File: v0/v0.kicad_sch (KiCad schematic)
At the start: 43 parts, among them CON1 SNES-CONN, M1 LY68L6400SLIT, U1 SN74LV165APWR, U2 SN74LV165APWR, U3 SN74LV165APWR, U4 SN74LVC8T245PWR, U5 PIC12F629-I/SN, U6 AMS1117-3.3, U7 SN74LVC8T245PWR, U8 Pair of 20-pin 1.27mm pitch v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

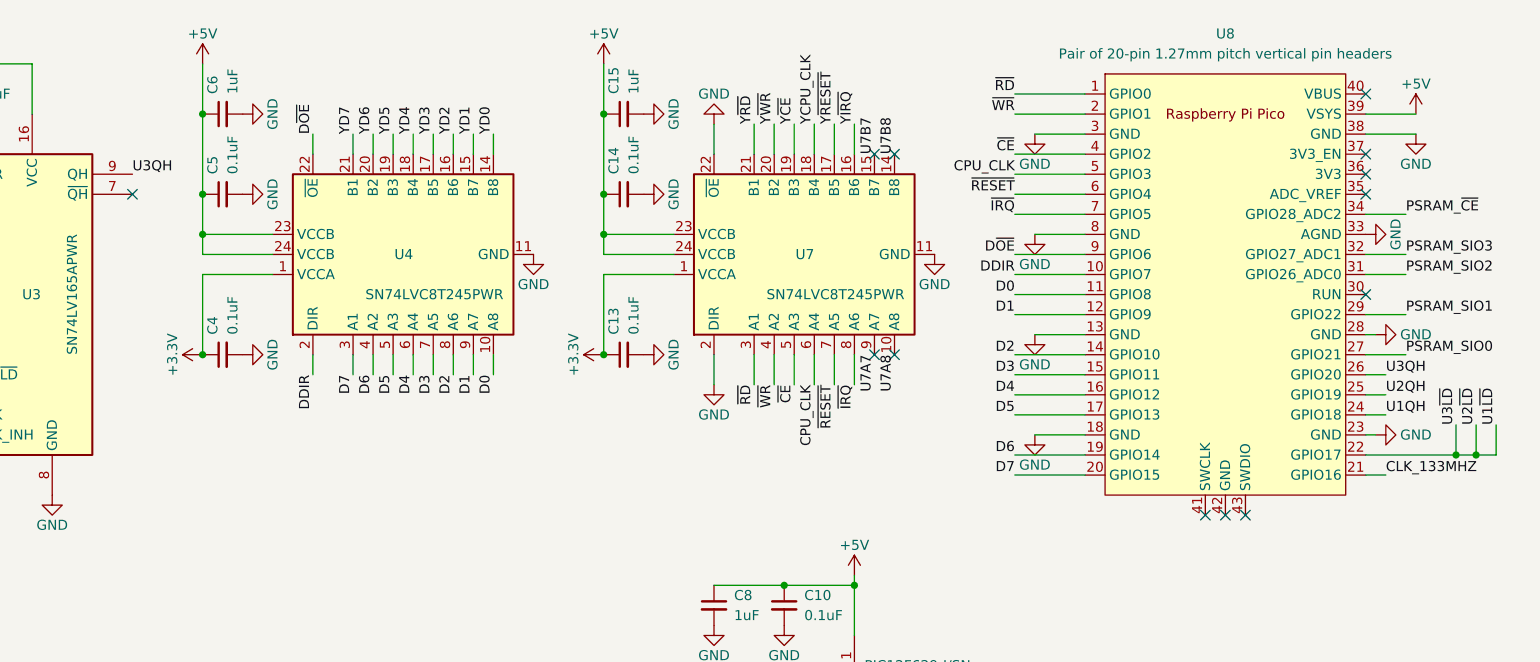
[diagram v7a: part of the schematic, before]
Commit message: Fix resistor array footprints and reroute; new layout of GPIO pins for PSRAM vs SNES address to be contiguous pin numbers
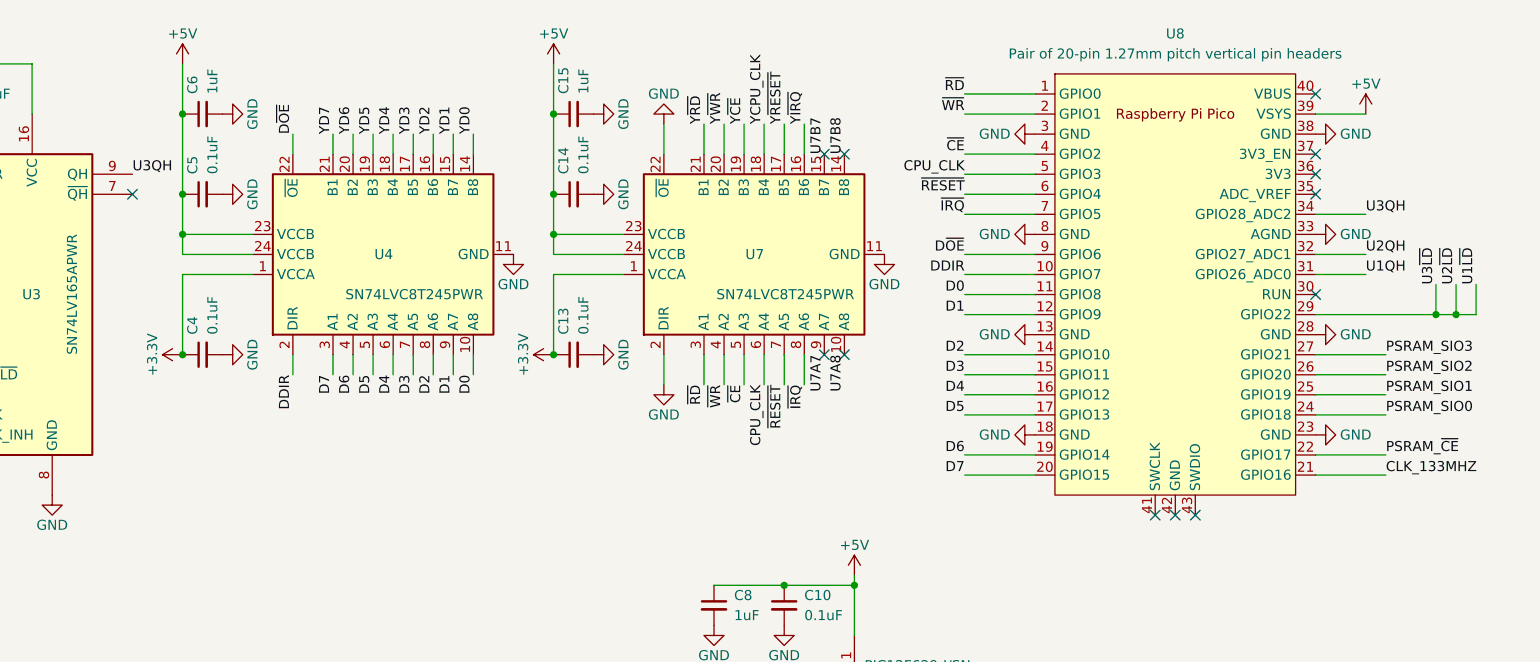
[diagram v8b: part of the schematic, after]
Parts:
- C1, C10, C11, C12, C13, C14, C15, C2, C3, C4, C5, C6, C7, C8, C9: JLC 1206_C -> 1206
- RN1, RN10, RN11, RN12, RN13, RN14, RN2, RN3, RN4, RN5, RN6, RN7, RN8, RN9: footprint Resistor_SMD:R_Array_Convex_4x1206 -> Resistor_SMD:R_Array_Concave_4x0603; JLC RES-ARRAY-SMD -> 0603_x4; LCSC C149863 -> C79203
- U6: LCSC C6186 -> C426566
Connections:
- net PSRAM_SIO0: now also U8.24 (GPIO18); no longer U8.27 (GPIO21)
- net PSRAM_SIO1: now also U8.25 (GPIO19); no longer U8.29 (GPIO22)
- net PSRAM_SIO2: now also U8.26 (GPIO20); no longer U8.31 (GPIO26_ADC0)
- net PSRAM_SIO3: now also U8.27 (GPIO21); no longer U8.32 (GPIO27_ADC1)
- net PSRAM_~{CE}: now also U8.22 (GPIO17); no longer U8.34 (GPIO28_ADC2)
- net U1QH: now also U8.31 (GPIO26_ADC0); no longer U8.24 (GPIO18)
- net U1~{LD}: now also U8.29 (GPIO22); no longer U8.22 (GPIO17)
- net U2QH: now also U8.32 (GPIO27_ADC1); no longer U8.25 (GPIO19)
- net U3QH: now also U8.34 (GPIO28_ADC2); no longer U8.26 (GPIO20)
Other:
- moved on the sheet: C13, C14, C15, C4, C5, C6, U4, U7, U8
